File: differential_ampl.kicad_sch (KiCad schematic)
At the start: 10 parts, among them U3 LT1492

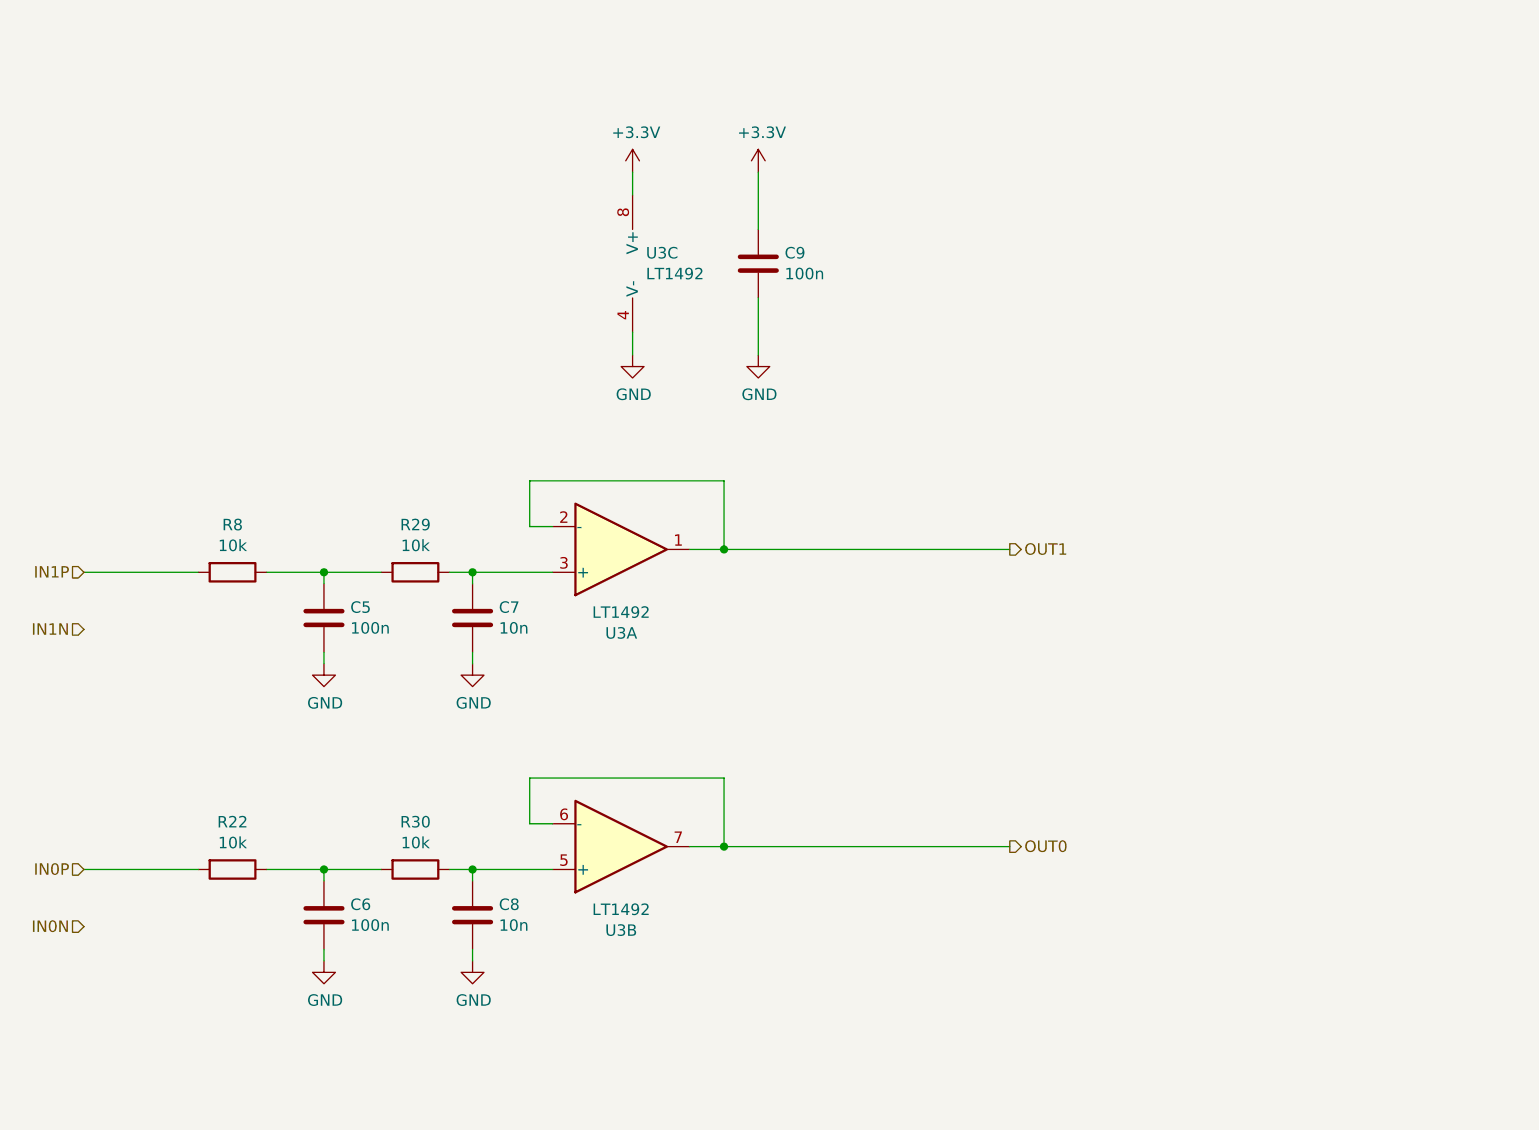
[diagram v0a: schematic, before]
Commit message: include a differential amplifier for allowing 4 wire connection
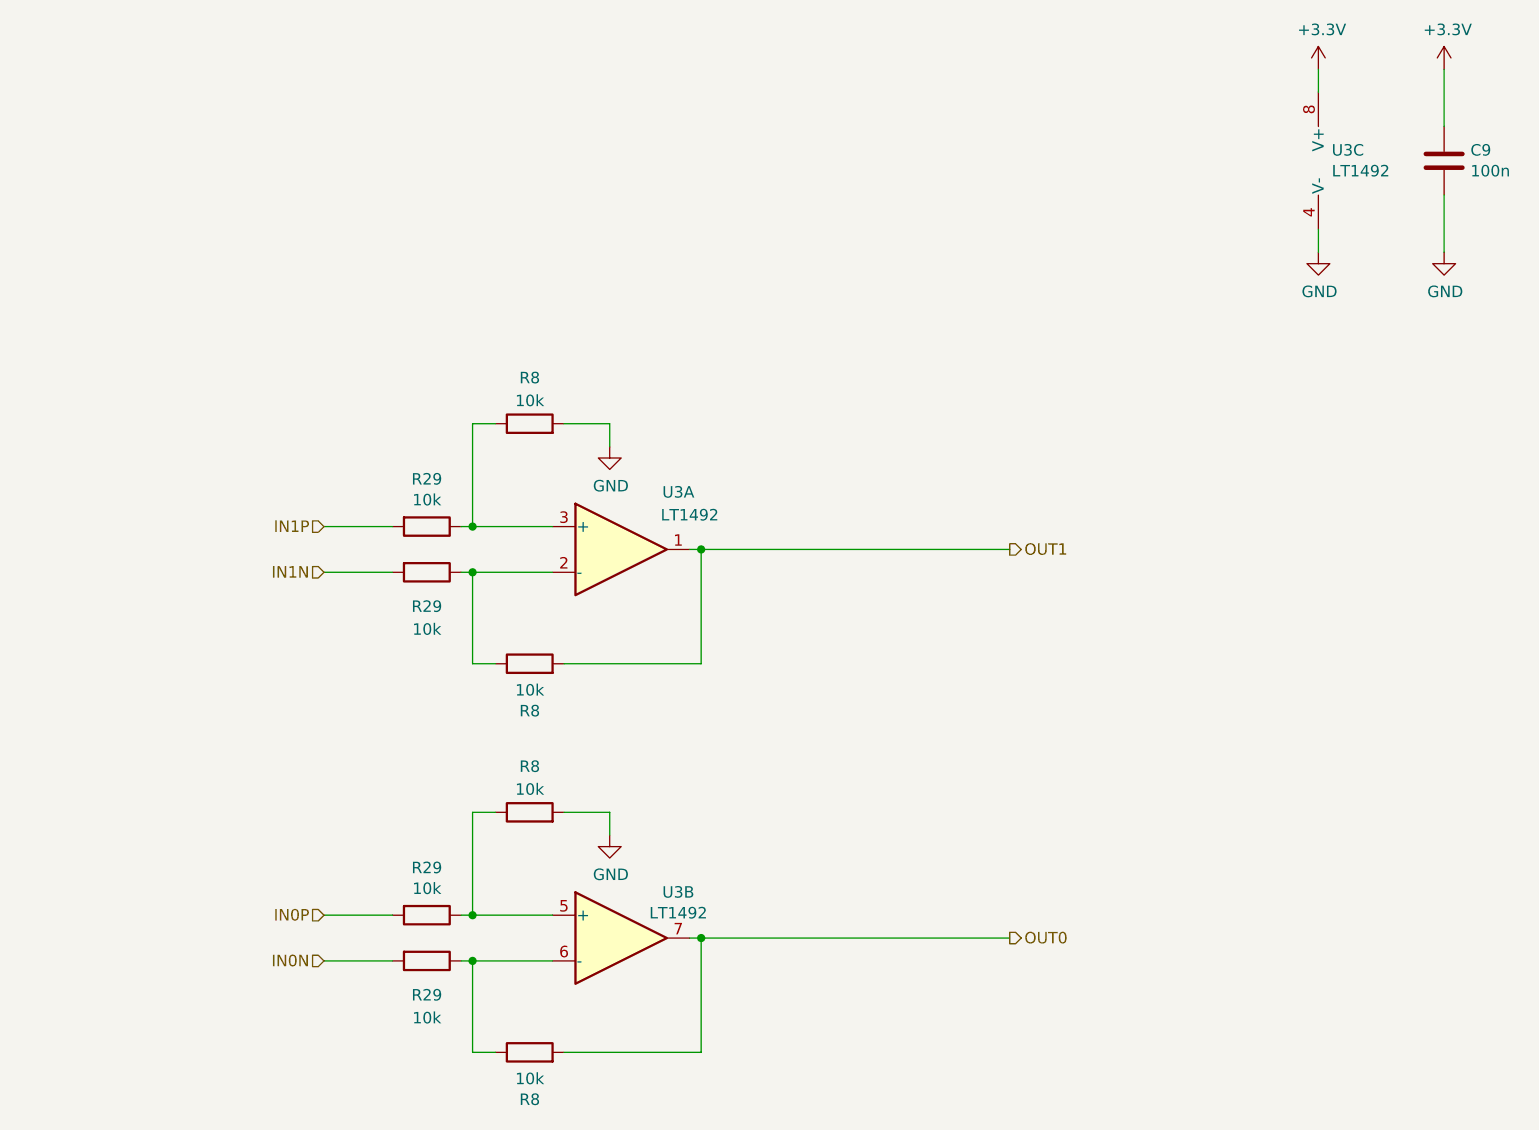
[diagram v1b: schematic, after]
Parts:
- removed C5, C6: 100n, Capacitor_SMD:C_0603_1608Metric, symbol Device:C
- removed C7, C8: 10n, Capacitor_SMD:C_0603_1608Metric, symbol Device:C
- removed R22, R30: 10k, Resistor_SMD:R_0603_1608Metric, symbol Device:R
- added R29 (x3), R8 (x3): 10k, Resistor_SMD:R_0603_1608Metric, symbol Device:R
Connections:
- net GND: now also R8.2, R8.2
- net IN0N: now also R29.2
- net IN0P: now also R29.2
- net IN1N: now also R29.2
- net IN1P: now also R29.2; no longer R8.2
- net OUT0: now also R8.2; no longer U3.6 (-)
- net OUT1: now also R8.2; no longer U3.2 (-)
- net at U3.5 (+): now also R29.1, R8.1
- net at R29.1: now also R8.1, U3.2 (-); no longer U3.3 (+)
- new net: R29.1, R8.1, U3.3 (+)
- new net: R29.1, R8.1, U3.6 (-)
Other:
- moved on the sheet: C9, R29, R8, U3B, U3C

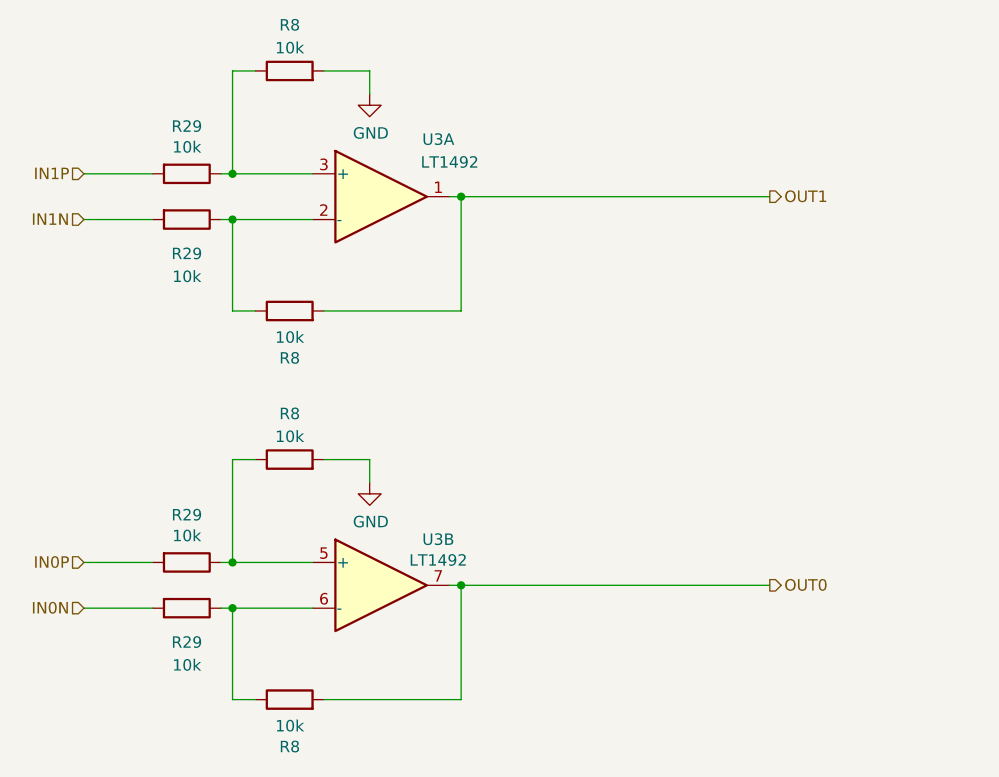
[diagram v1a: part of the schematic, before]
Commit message: added 4wire connection + differential amplifier to PCB
optimised layout and hence gained a bit more place for further extensions.
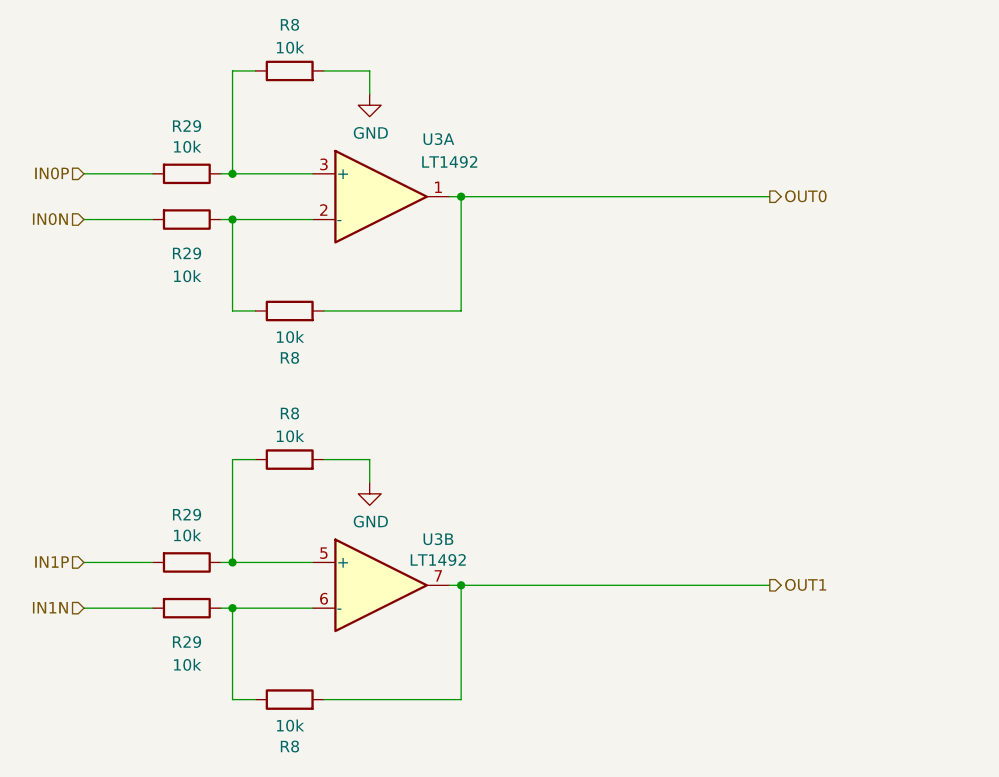
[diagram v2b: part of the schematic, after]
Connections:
- net IN0N: now also R29.2; no longer R29.2
- net IN0P: now also R29.2; no longer R29.2
- net IN1N: now also R29.2; no longer R29.2
- net IN1P: now also R29.2; no longer R29.2
- net OUT0: now also R8.2, U3.1; no longer R8.2, U3.7
- net OUT1: now also R8.2, U3.7; no longer R8.2, U3.1
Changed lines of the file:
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@@
     (stroke (width 0) (type default))
   )
-  (hierarchical_label "IN1P" (shape input) (at 115.57 83.82 180) (fields_autoplaced)
+  (hierarchical_label "IN1P" (shape input) (at 115.57 127 180) (fields_autoplaced)
     (effects (font (size 1.27 1.27)) (justify right))
   )
-  (hierarchical_label "IN0P" (shape input) (at 115.57 127 180) (fields_autoplaced)
+  (hierarchical_label "IN0P" (shape input) (at 115.57 83.82 180) (fields_autoplaced)
     (effects (font (size 1.27 1.27)) (justify right))
   )
-  (hierarchical_label "OUT0" (shape output) (at 191.77 129.54 0) (fields_autoplaced)
+  (hierarchical_label "OUT0" (shape output) (at 191.77 86.36 0) (fields_autoplaced)
     (effects (font (size 1.27 1.27)) (justify left))
   )
-  (hierarchical_label "IN1N" (shape input) (at 115.57 88.9 180) (fields_autoplaced)
+  (hierarchical_label "IN1N" (shape input) (at 115.57 132.08 180) (fields_autoplaced)
     (effects (font (size 1.27 1.27)) (justify right))
   )
-  (hierarchical_label "OUT1" (shape output) (at 191.77 86.36 0) (fields_autoplaced)
+  (hierarchical_label "OUT1" (shape output) (at 191.77 129.54 0) (fields_autoplaced)
     (effects (font (size 1.27 1.27)) (justify left))
   )
-  (hierarchical_label "IN0N" (shape input) (at 115.57 132.08 180) (fields_autoplaced)
+  (hierarchical_label "IN0N" (shape input) (at 115.57 88.9 180) (fields_autoplaced)
     (effects (font (size 1.27 1.27)) (justify right))
   )
